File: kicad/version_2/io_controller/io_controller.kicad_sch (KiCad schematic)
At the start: 20 parts

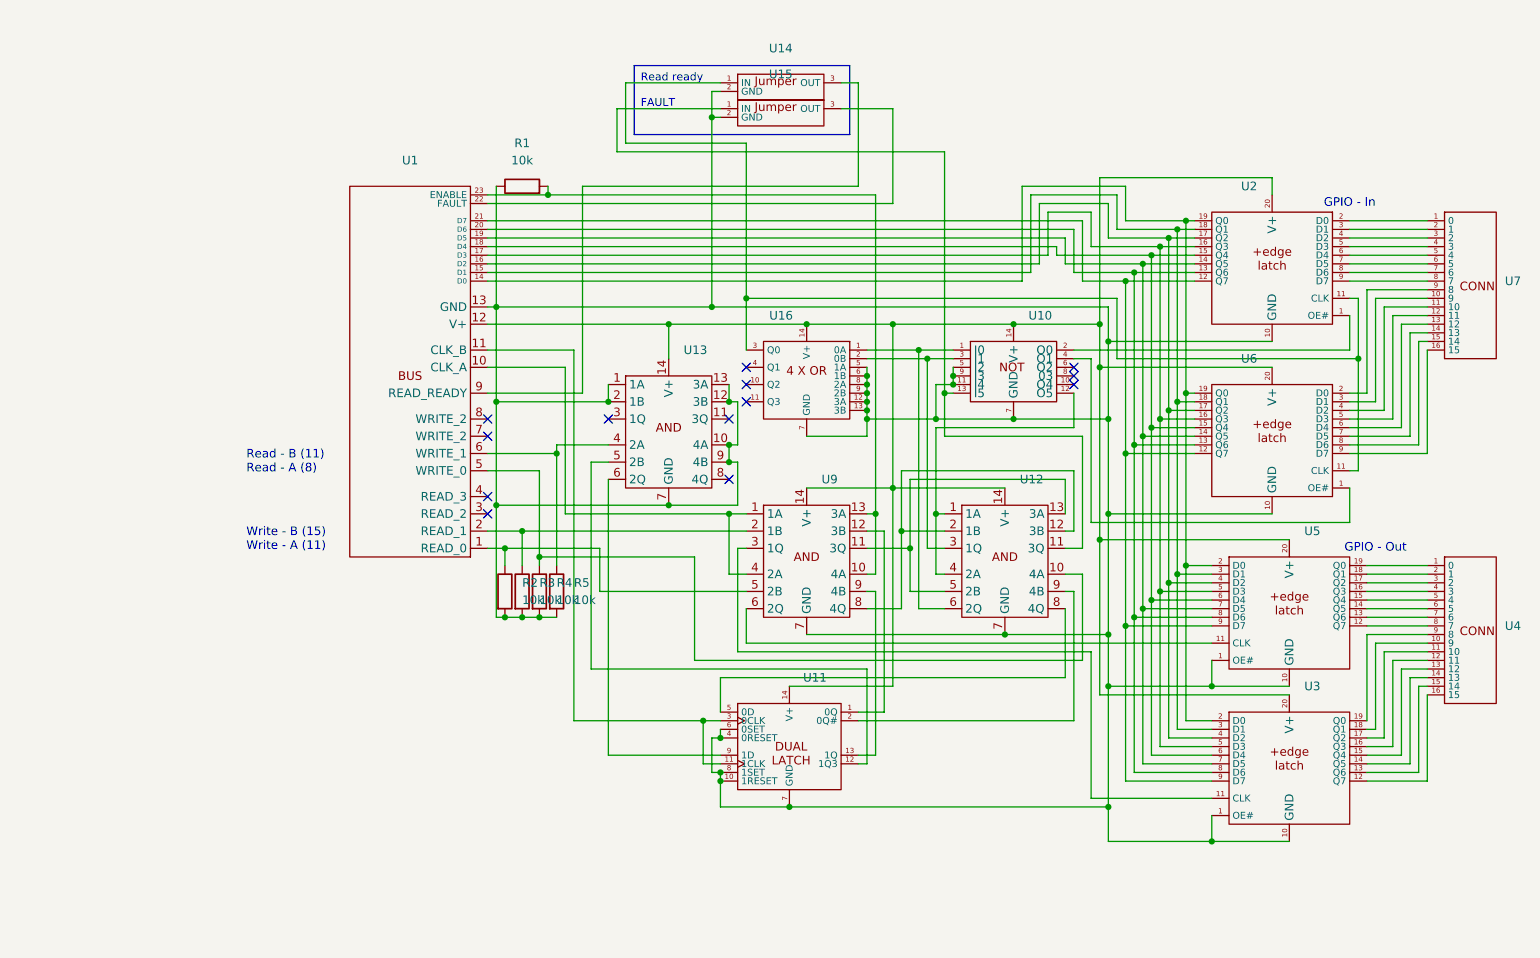
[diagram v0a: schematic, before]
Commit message: Added connector on IO controller to support display
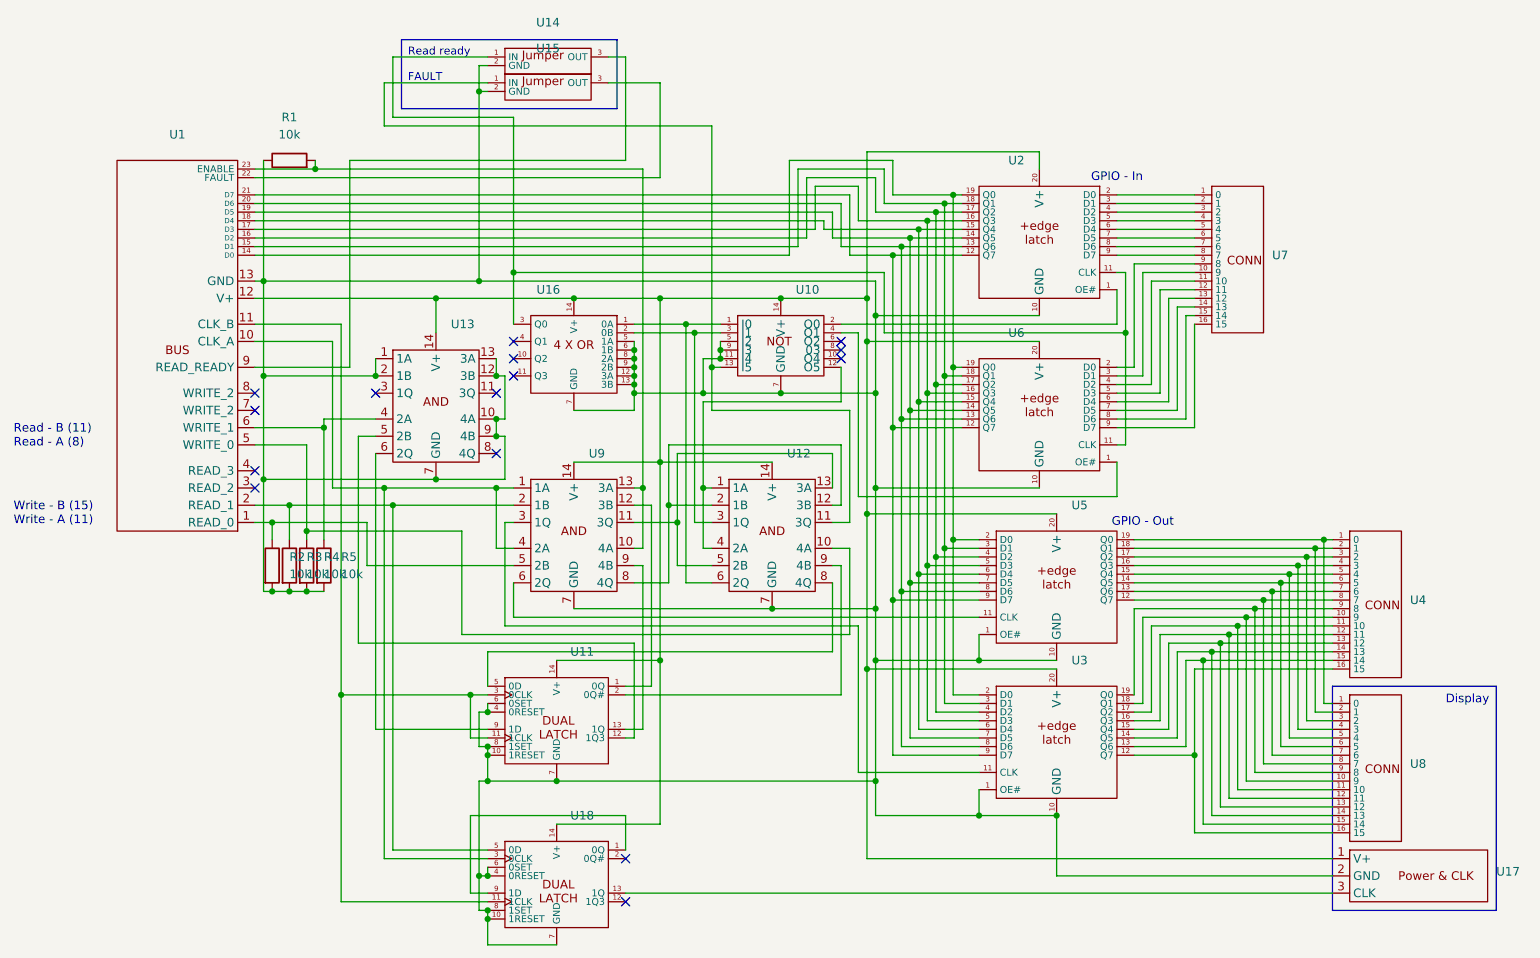
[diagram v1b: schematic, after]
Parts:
- added U17: ~, Connector_PinHeader_2.54mm:PinHeader_1x03_P2.54mm_Vertical, symbol custom_symbol_lib:power_and_clk
- added U18: ~, Package_DIP:DIP-14_W7.62mm, symbol custom_symbol_lib:dual_latch
- added U8: ~, Connector_PinHeader_2.54mm:PinHeader_1x16_P2.54mm_Vertical, symbol custom_symbol_lib:connector_16_bit
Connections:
- net at R1.1, R2.2, R3.2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: now also U17.2 (GND), U18.10 (1RESET), U18.4 (0RESET), U18.6 (0SET), U18.7 (GND), U18.8 (1SET)
- net at U4.1 (0), U5.19 (Q0): now also U8.1 (0)
- net at U3.18 (Q1), U4.10 (9): now also U8.10 (9)
- net at U3.17 (Q2), U4.11 (10): now also U8.11 (10)
- net at U3.16 (Q3), U4.12 (11): now also U8.12 (11)
- net at U3.15 (Q4), U4.13 (12): now also U8.13 (12)
- net at U3.14 (Q5), U4.14 (13): now also U8.14 (13)
- net at U3.13 (Q6), U4.15 (14): now also U8.15 (14)
- net at U3.12 (Q7), U4.16 (15): now also U8.16 (15)
- net at U4.2 (1), U5.18 (Q1): now also U8.2 (1)
- net at U4.3 (2), U5.17 (Q2): now also U8.3 (2)
- net at U4.4 (3), U5.16 (Q3): now also U8.4 (3)
- net at U4.5 (4), U5.15 (Q4): now also U8.5 (4)
- net at U4.6 (5), U5.14 (Q5): now also U8.6 (5)
- net at U4.7 (6), U5.13 (Q6): now also U8.7 (6)
- net at U4.8 (7), U5.12 (Q7): now also U8.8 (7)
- net at U3.19 (Q0), U4.9 (8): now also U8.9 (8)
- net at U1.12 (V+), U10.14 (V+), U11.14 (V+)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: now also U17.1 (V+), U18.14 (V+)
- net at R3.1, U1.2 (READ_1), U9.2 (1B): now also U18.5 (0D)
- net at U1.10 (CLK_A), U9.1 (1A), U9.4 (2A): now also U18.3 (0CLK)
- net at U1.11 (CLK_B), U11.11 (1CLK), U11.3 (0CLK): now also U18.11 (1CLK)
- new net: U18.1 (0Q), U18.9 (1D)
- new net: U17.3 (CLK), U18.13 (1Q)
- no-connect marks 13 -> 15
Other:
- moved on the sheet: R1, R2, R3, R4, R5, U1, U10, U11, U12, U13, U14, U15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
